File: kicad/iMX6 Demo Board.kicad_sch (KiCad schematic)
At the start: 0 parts

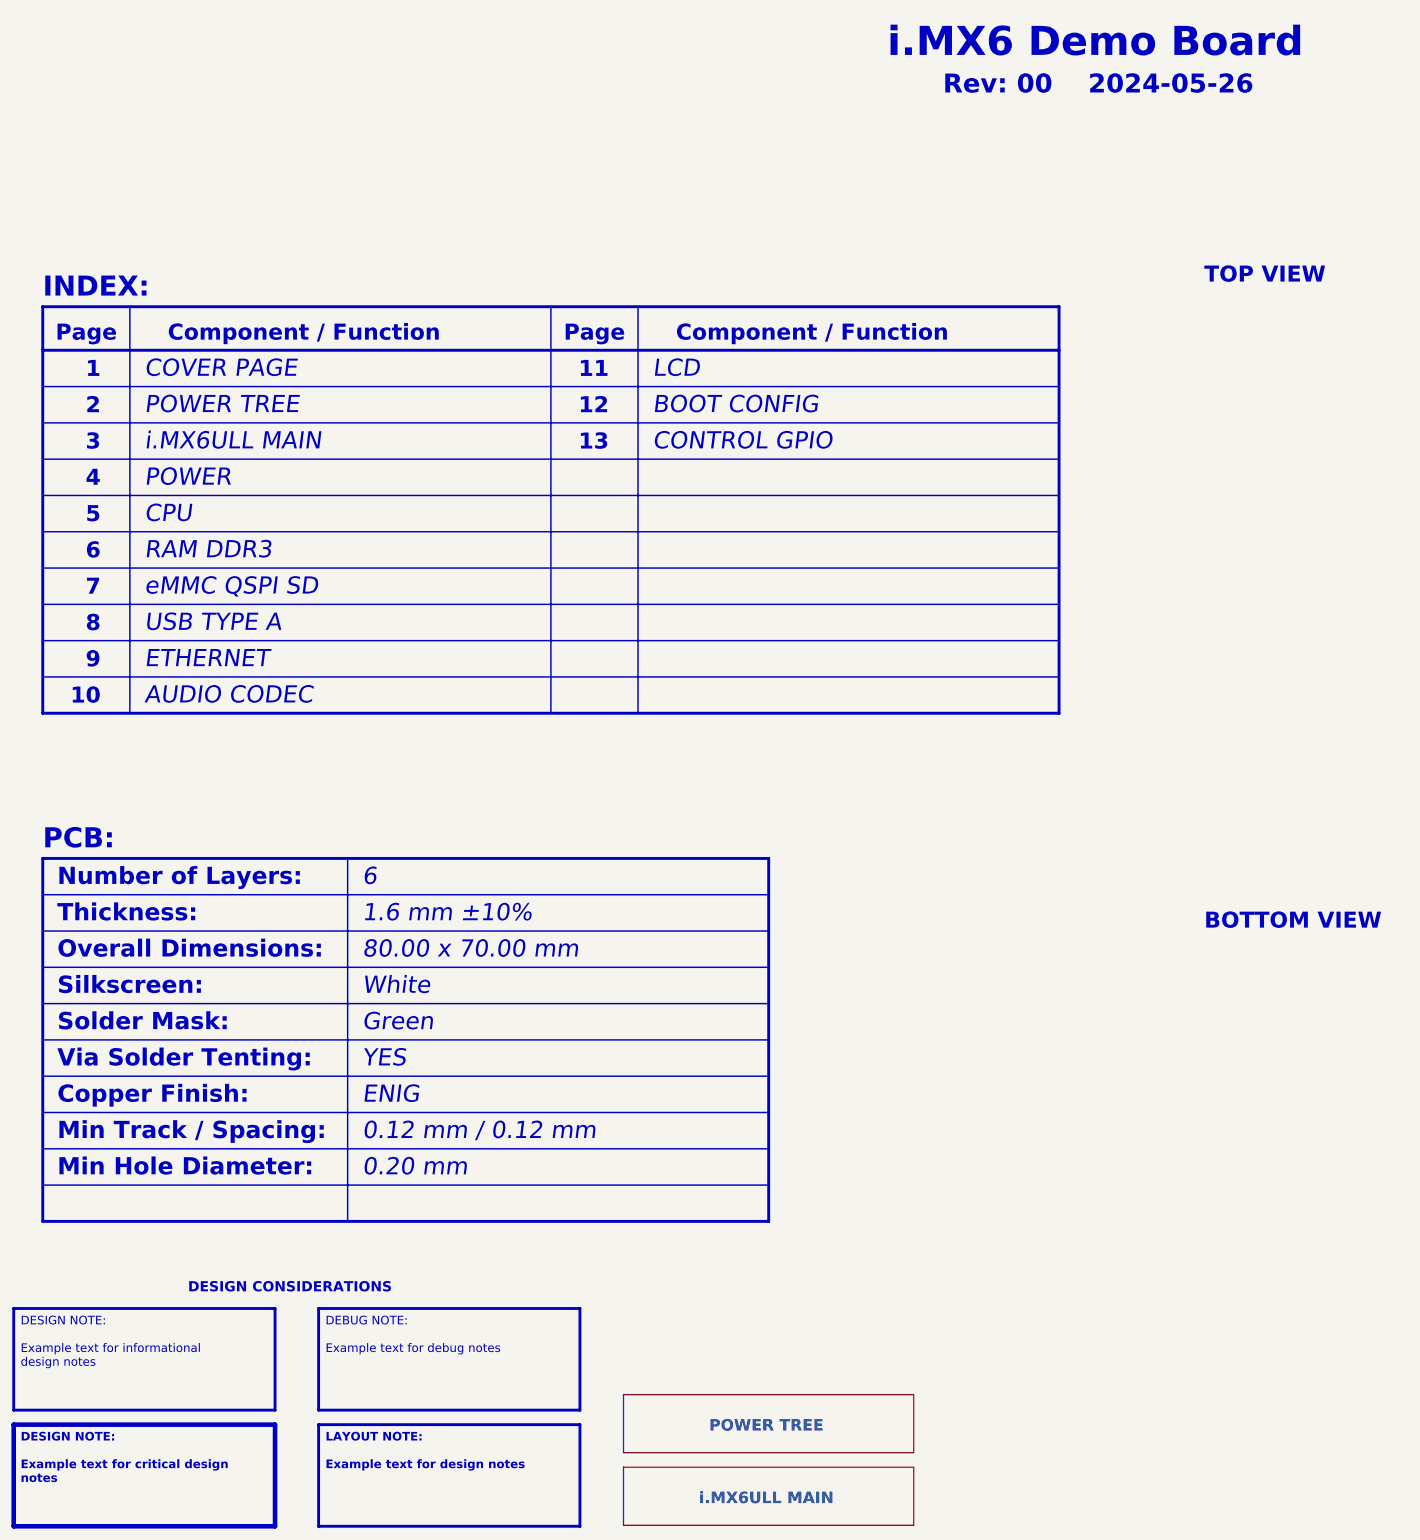
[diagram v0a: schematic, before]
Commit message: Fix hardware bugs - Fix part number in bom for resistors R103, R113, R114, R118 -> 680K - Fix part number in BOM for resistors R13, R16 -> 68K - Fix part number in BOM for resistor R14 -> 4.7K - Fix part number in BOM for capacitors C100, C101, C12, C13, C130, C131, C133, C135, C140, C141, C15, C19, C57, C58, C7, C99 -> 100nF - Fix footprint for USB-A connectors - Fix power buttom pull-up resistor connection -> connect to +3.3V_STAND_BY
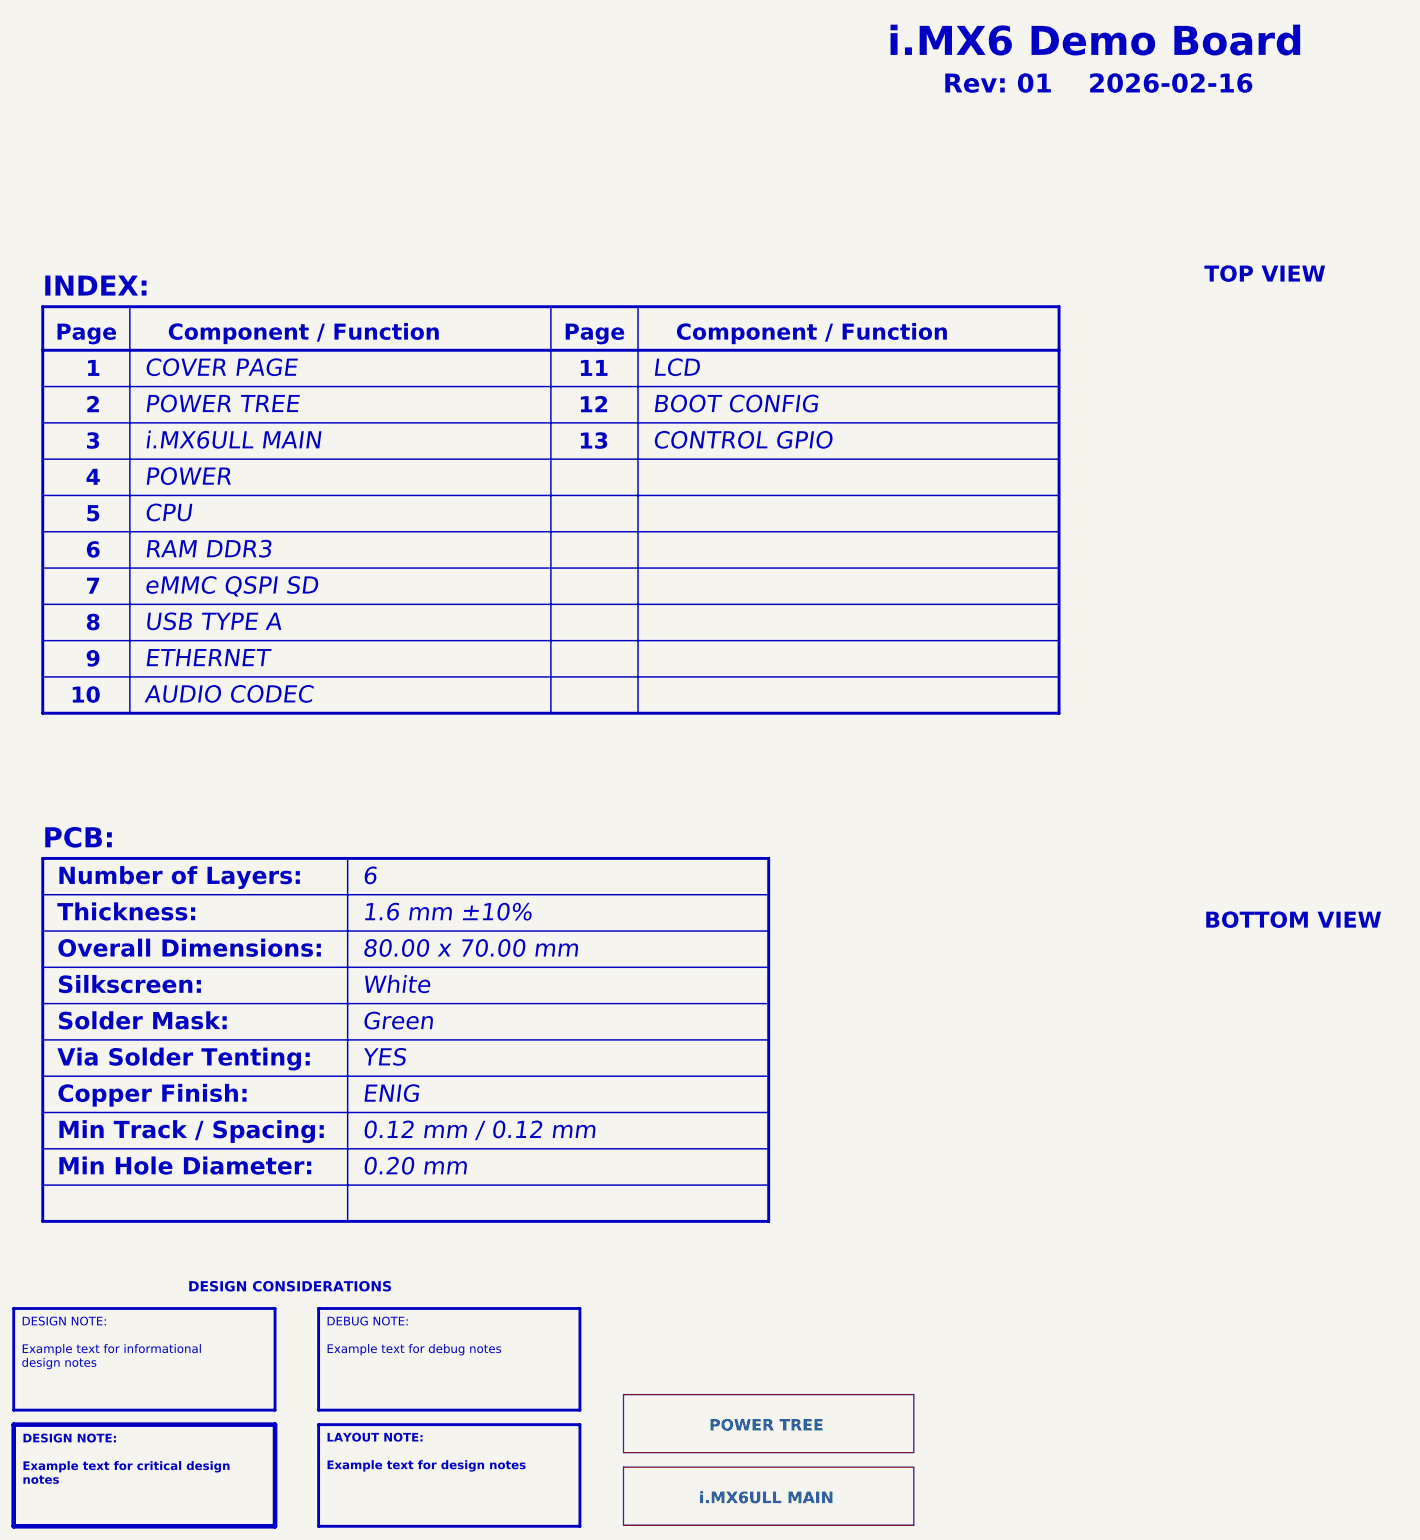
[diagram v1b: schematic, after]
